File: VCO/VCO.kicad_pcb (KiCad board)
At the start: 2 copper layers, 162.2 x 104.5 mm, 151 parts, among them J101 Conn_02x05_Odd_Even, J201 AudioJack2_SwitchT, J202 AudioJack2_SwitchT, J203 AudioJack2_SwitchT, J204 AudioJack2_SwitchT, J301 AudioJack2_SwitchT, J401 AudioJack2_SwitchT, J402 AudioJack2_SwitchT, J501 AudioJack2_SwitchT, J502 AudioJack2_SwitchT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

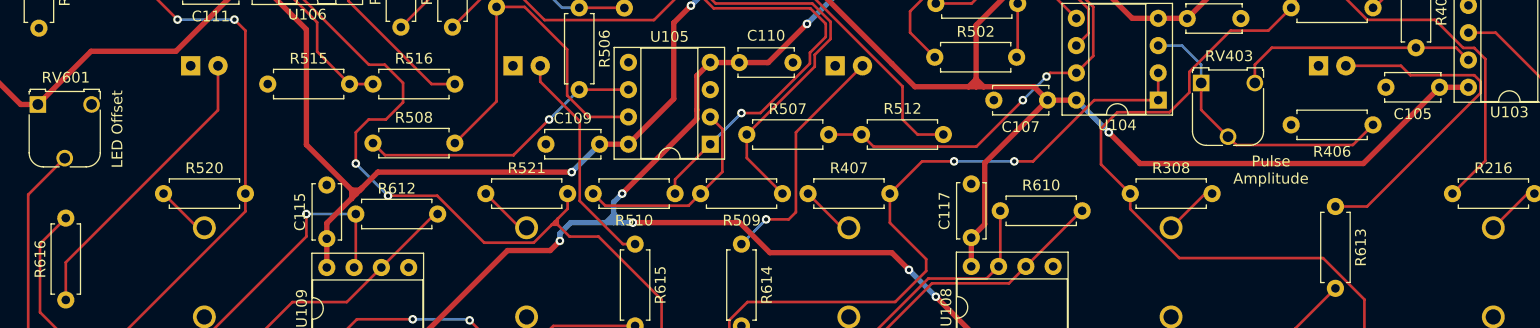
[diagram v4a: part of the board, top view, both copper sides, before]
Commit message: Flip VCO LEDs
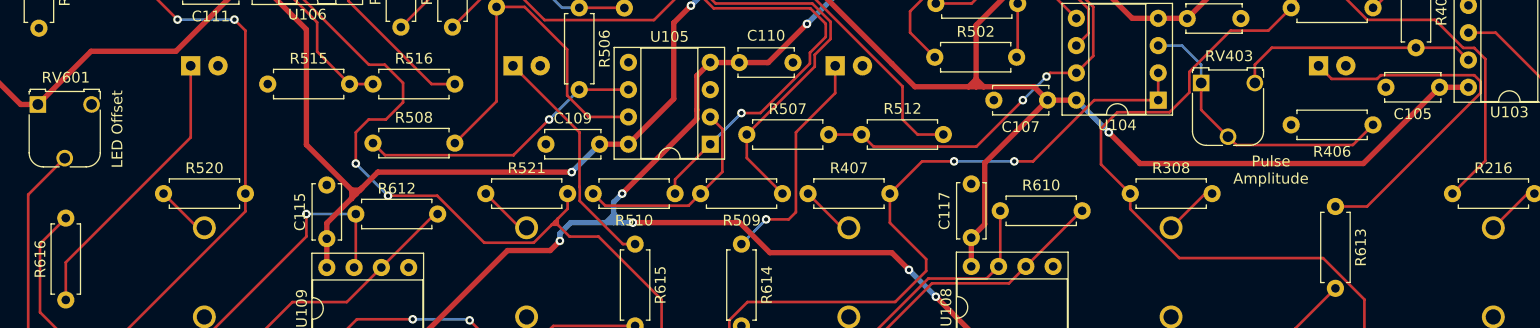
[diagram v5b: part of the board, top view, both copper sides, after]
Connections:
- D601 pad 1: GND -> Net-(R613-Pad1)
- D601 pad 2: Net-(D601-Pad2) -> GND
- D602 pad 1: GND -> Net-(R614-Pad1)
- D602 pad 2: Net-(D602-Pad2) -> GND
- D603 pad 1: GND -> Net-(R615-Pad1)
- D603 pad 2: Net-(D603-Pad2) -> GND
- D604 pad 1: GND -> Net-(R616-Pad1)
- D604 pad 2: Net-(D604-Pad2) -> GND
- R613 pad 1: Net-(D601-Pad2) -> Net-(R613-Pad1)
- R614 pad 1: Net-(D602-Pad2) -> Net-(R614-Pad1)
- R615 pad 1: Net-(D603-Pad2) -> Net-(R615-Pad1)
- R616 pad 1: Net-(D604-Pad2) -> Net-(R616-Pad1)
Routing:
- net Net-(R613-Pad1): track 0.00 -> 34.9 mm
- net Net-(D601-Pad2): track 32.1 -> 0.00 mm
- net Net-(D604-Pad2): track 27.7 -> 0.00 mm
- net Net-(R616-Pad1): track 0.00 -> 26.6 mm
- net Net-(D602-Pad2): track 22.5 -> 0.00 mm, vias 1 -> 0
- net Net-(R615-Pad1): track 0.00 -> 22.0 mm
- net Net-(R614-Pad1): track 0.00 -> 21.4 mm, vias 0 -> 1
- net Net-(D603-Pad2): track 20.9 -> 0.00 mm
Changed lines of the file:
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@@
   (net 16 "Net-(D502-Pad1)")
   (net 17 "Net-(D502-Pad2)")
-  (net 18 "Net-(D601-Pad2)")
-  (net 19 "Net-(D602-Pad2)")
-  (net 20 "Net-(D603-Pad2)")
-  (net 21 "Net-(D604-Pad2)")
+  (net 18 "Net-(R613-Pad1)")
+  (net 19 "Net-(R614-Pad1)")
+  (net 20 "Net-(R615-Pad1)")
+  (net 21 "Net-(R616-Pad1)")
   (net 22 "Net-(D501-Pad2)")
   (net 23 "unconnected-(J201-PadTN)")
@@
     (fp_line (start 7.62 0) (end 6.96 0) (layer "F.Fab") (width 0.1))
     (pad "1" thru_hole circle locked (at 0 0 270) (size 1.6 1.6) (drill 0.8) (layers *.Cu *.Mask)
-      (net 18 "Net-(D601-Pad2)") (pintype "passive"))
+      (net 18 "Net-(R613-Pad1)") (pintype "passive"))
     (pad "2" thru_hole oval locked (at 7.62 0 270) (size 1.6 1.6) (drill 0.8) (layers *.Cu *.Mask)
       (net 89 "Net-(R609-Pad1)") (pintype "passive"))
@@
     (fp_line (start 6.96 1.25) (end 6.96 -1.25) (layer "F.Fab") (width 0.1))
     (pad "1" thru_hole circle locked (at 0 0 270) (size 1.6 1.6) (drill 0.8) (layers *.Cu *.Mask)
-      (net 19 "Net-(D602-Pad2)") (pintype "passive"))
+      (net 19 "Net-(R614-Pad1)") (pintype "passive"))
     (pad "2" thru_hole oval locked (at 7.62 0 270) (size 1.6 1.6) (drill 0.8) (layers *.Cu *.Mask)
       (net 90 "Net-(R610-Pad1)") (pintype "passive"))
@@
     (fp_line (start 0.66 -1.25) (end 0.66 1.25) (layer "F.Fab") (width 0.1))
     (pad "1" thru_hole circle locked (at 0 0 270) (size 1.6 1.6) (drill 0.8) (layers *.Cu *.Mask)
-      (net 20 "Net-(D603-Pad2)") (pintype "passive"))
+      (net 20 "Net-(R615-Pad1)") (pintype "passive"))
     (pad "2" thru_hole oval locked (at 7.62 0 270) (size 1.6 1.6) (drill 0.8) (layers *.Cu *.Mask)
       (net 91 "Net-(R611-Pad1)") (pintype "passive"))
@@
     (fp_line (start 6.96 -1.25) (end 0.66 -1.25) (layer "F.Fab") (width 0.1))
     (pad "1" thru_hole circle locked (at 0 0 90) (size 1.6 1.6) (drill 0.8) (layers *.Cu *.Mask)
-      (net 21 "Net-(D604-Pad2)") (pintype "passive"))
+      (net 21 "Net-(R616-Pad1)") (pintype "passive"))
     (pad "2" thru_hole oval locked (at 7.62 0 90) (size 1.6 1.6) (drill 0.8) (layers *.Cu *.Mask)
       (net 92 "Net-(R612-Pad1)") (pintype "passive"))
@@
     (fp_circle (center 1.27 0) (end 3.77 0) (layer "B.Fab") (width 0.1) (fill none))
     (pad "1" thru_hole rect locked (at 0 0) (size 1.8 1.8) (drill 0.9) (layers *.Cu *.Mask)
-      (net 1 "GND") (pinfunction "K") (pintype "passive"))
+      (net 18 "Net-(R613-Pad1)") (pinfunction "K") (pintype "passive"))
     (pad "2" thru_hole circle locked (at 2.54 0) (size 1.8 1.8) (drill 0.9) (layers *.Cu *.Mask)
-      (net 18 "Net-(D601-Pad2)") (pinfunction "A") (pintype "passive"))
+      (net 1 "GND") (pinfunction "A") (pintype "passive"))
     (model "${KISYS3DMOD}/LED_THT.3dshapes/LED_D5.0mm.wrl"
       (offset (xyz 0 0 0))
@@
     (fp_circle (center 1.27 0) (end 3.77 0) (layer "B.Fab") (width 0.1) (fill none))
     (pad "1" thru_hole rect locked (at 0 0) (size 1.8 1.8) (drill 0.9) (layers *.Cu *.Mask)
-      (net 1 "GND") (pinfunction "K") (pintype "passive"))
+      (net 19 "Net-(R614-Pad1)") (pinfunction "K") (pintype "passive"))
     (pad "2" thru_hole circle locked (at 2.54 0) (size 1.8 1.8) (drill 0.9) (layers *.Cu *.Mask)
-      (net 19 "Net-(D602-Pad2)") (pinfunction "A") (pintype "passive"))
+      (net 1 "GND") (pinfunction "A") (pintype "passive"))
     (model "${KISYS3DMOD}/LED_THT.3dshapes/LED_D5.0mm.wrl"
       (offset (xyz 0 0 0))
@@
     (fp_circle (center 1.27 0) (end 3.77 0) (layer "B.Fab") (width 0.1) (fill none))
     (pad "1" thru_hole rect locked (at 0 0) (size 1.8 1.8) (drill 0.9) (layers *.Cu *.Mask)
-      (net 1 "GND") (pinfunction "K") (pintype "passive"))
+      (net 20 "Net-(R615-Pad1)") (pinfunction "K") (pintype "passive"))
     (pad "2" thru_hole circle locked (at 2.54 0) (size 1.8 1.8) (drill 0.9) (layers *.Cu *.Mask)
-      (net 20 "Net-(D603-Pad2)") (pinfunction "A") (pintype "passive"))
+      (net 1 "GND") (pinfunction "A") (pintype "passive"))
     (model "${KISYS3DMOD}/LED_THT.3dshapes/LED_D5.0mm.wrl"
       (offset (xyz 0 0 0))
@@
     (fp_circle (center 1.27 0) (end 3.77 0) (layer "B.Fab") (width 0.1) (fill none))
     (pad "1" thru_hole rect locked (at 0 0) (size 1.8 1.8) (drill 0.9) (layers *.Cu *.Mask)
-      (net 1 "GND") (pinfunction "K") (pintype "passive"))
+      (net 21 "Net-(R616-Pad1)") (pinfunction "K") (pintype "passive"))
     (pad "2" thru_hole circle locked (at 2.54 0) (size 1.8 1.8) (drill 0.9) (layers *.Cu *.Mask)
-      (net 21 "Net-(D604-Pad2)") (pinfunction "A") (pintype "passive"))
+      (net 1 "GND") (pinfunction "A") (pintype "passive"))
     (model "${KISYS3DMOD}/LED_THT.3dshapes/LED_D5.0mm.wrl"
       (offset (xyz 0 0 0))
@@
   (segment (start 113.3 113.62) (end 113.3 104.82) (width 0.25) (layer "F.Cu") (net 17))
   (segment (start 113.3 104.82) (end 115.92 104.82) (width 0.25) (layer "F.Cu") (net 17))
-  (segment (start 204.320001 111.174999) (end 204.905001 111.759999) (width 0.25) (layer "F.Cu") (net 18))
-  (segment (start 204.905001 111.759999) (end 204.905001 112.840001) (width 0.25) (layer "F.Cu") (net 18))
-  (segment (start 197.5 110.3) (end 198.374999 111.174999) (width 0.25) (layer "F.Cu") (net 18))
   (segment (start 194.345002 123.4) (end 191.4 123.4) (width 0.25) (layer "F.Cu") (net 18))
-  (segment (start 192.37 110.3) (end 197.5 110.3) (width 0.25) (layer "F.Cu") (net 18))
-  (segment (start 198.374999 111.174999) (end 204.320001 111.174999) (width 0.25) (layer "F.Cu") (net 18))
   (segment (start 204.905001 112.840001) (end 194.345002 123.4) (width 0.25) (layer "F.Cu") (net 18))
-  (segment (start 141.174999 116.495001) (end 147.37 110.3) (width 0.25) (layer "F.Cu") (net 19))
+  (segment (start 204.905001 111.759999) (end 204.905001 112.840001) (width 0.25) (layer "F.Cu") (net 18))
+  (segment (start 191.054511 111.524511) (end 195.275489 111.524511) (width 0.25) (layer "F.Cu") (net 18))
+  (segment (start 195.625001 111.174999) (end 204.320001 111.174999) (width 0.25) (layer "F.Cu") (net 18))
+  (segment (start 189.83 110.3) (end 191.054511 111.524511) (width 0.25) (layer "F.Cu") (net 18))
+  (segment (start 204.320001 111.174999) (end 204.905001 111.759999) (width 0.25) (layer "F.Cu") (net 18))
+  (segment (start 195.275489 111.524511) (end 195.625001 111.174999) (width 0.25) (layer "F.Cu") (net 18))
   (segment (start 138.4 124.6) (end 140.5 124.6) (width 0.25) (layer "F.Cu") (net 19))
+  (segment (start 141.174999 116.495001) (end 144.83 112.84) (width 0.25) (layer "F.Cu") (net 19))
   (segment (start 140.5 124.6) (end 141.174999 123.925001) (width 0.25) (layer "F.Cu") (net 19))
   (segment (start 141.174999 123.925001) (end 141.174999 116.495001) (width 0.25) (layer "F.Cu") (net 19))
+  (segment (start 144.83 112.84) (end 144.83 110.3) (width 0.25) (layer "F.Cu") (net 19))
   (via (at 138.4 124.6) (size 0.8) (drill 0.4) (layers "F.Cu" "B.Cu") (net 19))
   (segment (start 136.1 126.9) (end 138.4 124.6) (width 0.25) (layer "B.Cu") (net 19))
+  (segment (start 121.024511 116.494511) (end 121.024511 121.575489) (width 0.25) (layer "F.Cu") (net 20))
+  (segment (start 121.024511 121.575489) (end 121.045001 121.595979) (width 0.25) (layer "F.Cu") (net 20))
   (segment (start 126.2 126.9) (end 125.06863 126.9) (width 0.25) (layer "F.Cu") (net 20))
-  (segment (start 121.045001 122.876371) (end 121.045001 115.445001) (width 0.25) (layer "F.Cu") (net 20))
+  (segment (start 114.83 110.3) (end 121.024511 116.494511) (width 0.25) (layer "F.Cu") (net 20))
   (segment (start 125.06863 126.9) (end 121.045001 122.876371) (width 0.25) (layer "F.Cu") (net 20))
-  (segment (start 117.37 111.77) (end 117.37 110.3) (width 0.25) (layer "F.Cu") (net 20))
-  (segment (start 121.045001 115.445001) (end 117.37 111.77) (width 0.25) (layer "F.Cu") (net 20))
-  (segment (start 73.2 128.6) (end 87.37 114.43) (width 0.25) (layer "F.Cu") (net 21))
+  (segment (start 121.045001 121.595979) (end 121.045001 122.876371) (width 0.25) (layer "F.Cu") (net 20))
   (segment (start 73.2 132.1) (end 73.2 128.6) (width 0.25) (layer "F.Cu") (net 21))
-  (segment (start 87.37 114.43) (end 87.37 110.3) (width 0.25) (layer "F.Cu") (net 21))
+  (segment (start 84.83 116.97) (end 84.83 110.3) (width 0.25) (layer "F.Cu") (net 21))
+  (segment (start 73.2 128.6) (end 84.83 116.97) (width 0.25) (layer "F.Cu") (net 21))
   (segment (start 116.7 102.2) (end 116.050978 102.2) (width 0.25) (layer "F.Cu") (net 22))
   (segment (start 125.18 104.9) (end 125.2 104.92) (width 0.25) (layer "F.Cu") (net 22))

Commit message: Add SKVCF
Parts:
- R202: value 8.2k -> 6.8k
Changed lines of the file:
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@@
   (net 16 "Net-(D502-Pad1)")
   (net 17 "Net-(D502-Pad2)")
-  (net 18 "Net-(R613-Pad1)")
-  (net 19 "Net-(R614-Pad1)")
-  (net 20 "Net-(R615-Pad1)")
-  (net 21 "Net-(R616-Pad1)")
+  (net 18 "Net-(D601-Pad1)")
+  (net 19 "Net-(D602-Pad1)")
+  (net 20 "Net-(D603-Pad1)")
+  (net 21 "Net-(D604-Pad1)")
   (net 22 "Net-(D501-Pad2)")
   (net 23 "unconnected-(J201-PadTN)")
@@
       (effects (font (size 1 1) (thickness 0.15)))
     )
-    (fp_text value "8.2k" (at 3.81 2.37) (layer "F.Fab")
+    (fp_text value "6.8k" (at 3.81 2.37) (layer "F.Fab")
       (effects (font (size 1 1) (thickness 0.15)))
     )
@@
     (fp_line (start 7.62 0) (end 6.96 0) (layer "F.Fab") (width 0.1))
     (pad "1" thru_hole circle locked (at 0 0 270) (size 1.6 1.6) (drill 0.8) (layers *.Cu *.Mask)
-      (net 18 "Net-(R613-Pad1)") (pintype "passive"))
+      (net 18 "Net-(D601-Pad1)") (pintype "passive"))
     (pad "2" thru_hole oval locked (at 7.62 0 270) (size 1.6 1.6) (drill 0.8) (layers *.Cu *.Mask)
       (net 89 "Net-(R609-Pad1)") (pintype "passive"))
@@
     (fp_line (start 6.96 1.25) (end 6.96 -1.25) (layer "F.Fab") (width 0.1))
     (pad "1" thru_hole circle locked (at 0 0 270) (size 1.6 1.6) (drill 0.8) (layers *.Cu *.Mask)
-      (net 19 "Net-(R614-Pad1)") (pintype "passive"))
+      (net 19 "Net-(D602-Pad1)") (pintype "passive"))
     (pad "2" thru_hole oval locked (at 7.62 0 270) (size 1.6 1.6) (drill 0.8) (layers *.Cu *.Mask)
       (net 90 "Net-(R610-Pad1)") (pintype "passive"))
@@
     (fp_line (start 0.66 -1.25) (end 0.66 1.25) (layer "F.Fab") (width 0.1))
     (pad "1" thru_hole circle locked (at 0 0 270) (size 1.6 1.6) (drill 0.8) (layers *.Cu *.Mask)
-      (net 20 "Net-(R615-Pad1)") (pintype "passive"))
+      (net 20 "Net-(D603-Pad1)") (pintype "passive"))
     (pad "2" thru_hole oval locked (at 7.62 0 270) (size 1.6 1.6) (drill 0.8) (layers *.Cu *.Mask)
       (net 91 "Net-(R611-Pad1)") (pintype "passive"))
@@
     (fp_line (start 6.96 -1.25) (end 0.66 -1.25) (layer "F.Fab") (width 0.1))
     (pad "1" thru_hole circle locked (at 0 0 90) (size 1.6 1.6) (drill 0.8) (layers *.Cu *.Mask)
-      (net 21 "Net-(R616-Pad1)") (pintype "passive"))
+      (net 21 "Net-(D604-Pad1)") (pintype "passive"))
     (pad "2" thru_hole oval locked (at 7.62 0 90) (size 1.6 1.6) (drill 0.8) (layers *.Cu *.Mask)
       (net 92 "Net-(R612-Pad1)") (pintype "passive"))
@@
     (fp_circle (center 1.27 0) (end 3.77 0) (layer "B.Fab") (width 0.1) (fill none))
     (pad "1" thru_hole rect locked (at 0 0) (size 1.8 1.8) (drill 0.9) (layers *.Cu *.Mask)
-      (net 18 "Net-(R613-Pad1)") (pinfunction "K") (pintype "passive"))
+      (net 18 "Net-(D601-Pad1)") (pinfunction "K") (pintype "passive"))
     (pad "2" thru_hole circle locked (at 2.54 0) (size 1.8 1.8) (drill 0.9) (layers *.Cu *.Mask)
       (net 1 "GND") (pinfunction "A") (pintype "passive"))
@@
     (fp_circle (center 1.27 0) (end 3.77 0) (layer "B.Fab") (width 0.1) (fill none))
     (pad "1" thru_hole rect locked (at 0 0) (size 1.8 1.8) (drill 0.9) (layers *.Cu *.Mask)
-      (net 19 "Net-(R614-Pad1)") (pinfunction "K") (pintype "passive"))
+      (net 19 "Net-(D602-Pad1)") (pinfunction "K") (pintype "passive"))
     (pad "2" thru_hole circle locked (at 2.54 0) (size 1.8 1.8) (drill 0.9) (layers *.Cu *.Mask)
       (net 1 "GND") (pinfunction "A") (pintype "passive"))
@@
     (fp_circle (center 1.27 0) (end 3.77 0) (layer "B.Fab") (width 0.1) (fill none))
     (pad "1" thru_hole rect locked (at 0 0) (size 1.8 1.8) (drill 0.9) (layers *.Cu *.Mask)
-      (net 20 "Net-(R615-Pad1)") (pinfunction "K") (pintype "passive"))
+      (net 20 "Net-(D603-Pad1)") (pinfunction "K") (pintype "passive"))
     (pad "2" thru_hole circle locked (at 2.54 0) (size 1.8 1.8) (drill 0.9) (layers *.Cu *.Mask)
       (net 1 "GND") (pinfunction "A") (pintype "passive"))
@@
     (fp_circle (center 1.27 0) (end 3.77 0) (layer "B.Fab") (width 0.1) (fill none))
     (pad "1" thru_hole rect locked (at 0 0) (size 1.8 1.8) (drill 0.9) (layers *.Cu *.Mask)
-      (net 21 "Net-(R616-Pad1)") (pinfunction "K") (pintype "passive"))
+      (net 21 "Net-(D604-Pad1)") (pinfunction "K") (pintype "passive"))
     (pad "2" thru_hole circle locked (at 2.54 0) (size 1.8 1.8) (drill 0.9) (layers *.Cu *.Mask)
       (net 1 "GND") (pinfunction "A") (pintype "passive"))
